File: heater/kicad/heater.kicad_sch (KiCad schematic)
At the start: 80 parts, among them J1 Conn_01x02_Pin, J2 Conn_01x02_Pin, J3 pcie_98, U1 OPA863SIDBVR, U11 ESD5344D-TP, U12 ESD5344D-TP, U13 XC6206P332MR, U14 B0505MT-1WR4, U15 TPS7A2025PDBVR, U16 LM27761, U3 LTC1968, U4 LTC1968, U8 ADS1115IDGS, U9 ISO1541

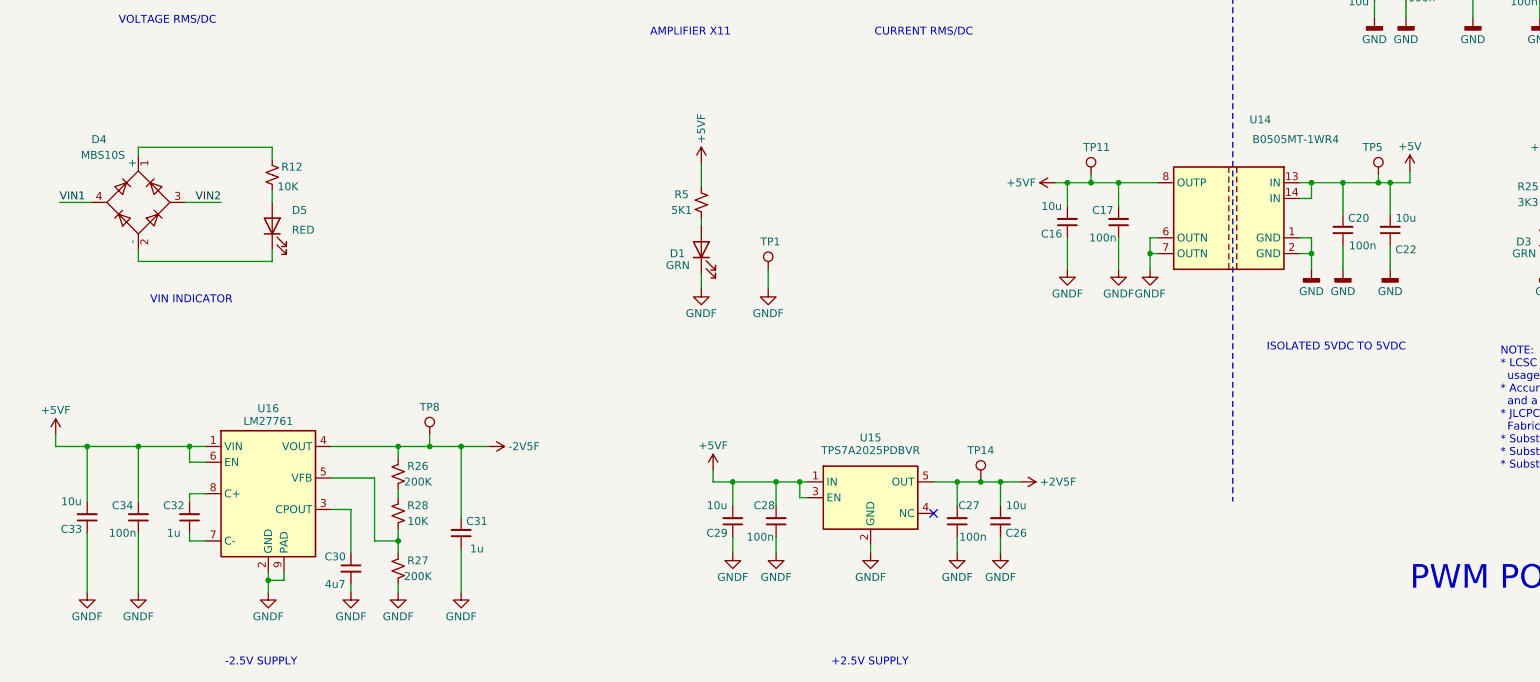
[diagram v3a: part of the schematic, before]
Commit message: Updated the heater schematic. Using +/-5V dc/dc instead of a charge pump.
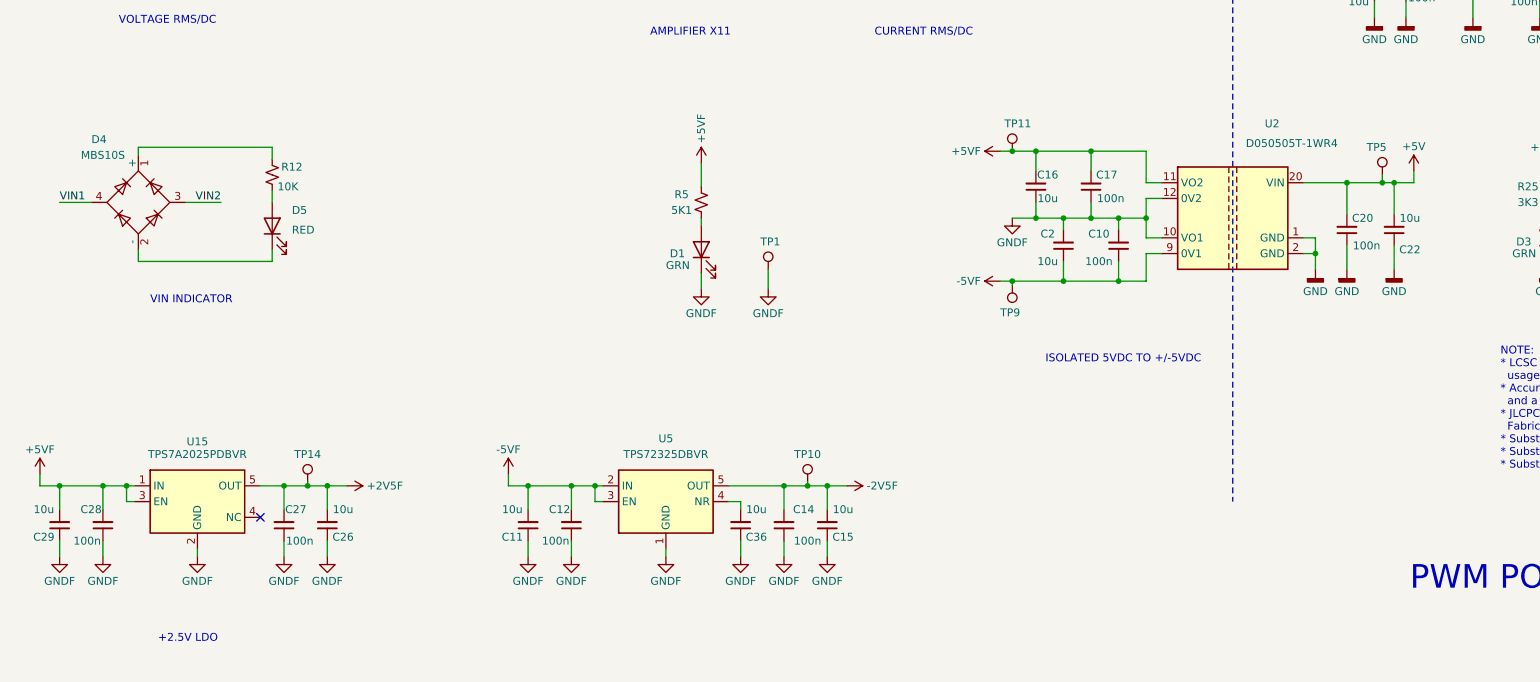
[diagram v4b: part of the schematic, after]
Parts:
- removed C30: 4u7, Capacitor_SMD:C_0402_1005Metric, symbol Device:C_Small
- removed C31, C32: 1u, Capacitor_SMD:C_0402_1005Metric, symbol Device:C_Small
- removed C33: 10u, Capacitor_SMD:C_0603_1608Metric, symbol Device:C_Small
- removed C34: 100n, Capacitor_SMD:C_0402_1005Metric, symbol Device:C_Small
- removed R26, R27: 200K, Resistor_SMD:R_0402_1005Metric, symbol Device:R_Small_US
- removed R28: 10K, Resistor_SMD:R_0402_1005Metric, symbol Device:R_Small_US
- removed TP8: TestPoint, common:Test_Pad, symbol common:TestPoint
- removed U14: B0505MT-1WR4, common:B0505MT-1WR4, symbol common:B0505MT-1WR4
- removed U16: LM27761, Package_SON:WSON-8-1EP_2x2mm_P0.5mm_EP0.9x1.6mm, symbol Regulator_SwitchedCapacitor:LM27761
- added C10, C12, C14: 100n, Capacitor_SMD:C_0402_1005Metric, symbol Device:C_Small
- added C11, C15, C2, C36: 10u, Capacitor_SMD:C_0603_1608Metric, symbol Device:C_Small
- added TP10, TP9: TestPoint, common:Test_Pad, symbol common:TestPoint
- added U2: D050505T-1WR4, common:D050505T-1WR4, symbol common:D050505T-1WR4
- added U5: TPS72325DBVR, Package_TO_SOT_SMD:SOT-23-5, symbol common:TPS72325DBVR
- U8: LCSC Digikey -> C37593
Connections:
- net +5V: now also U2.20 (VIN)
- net +5VF: now also U2.11 (VO2)
- net -2V5F: now also C14.2, C15.2, TP10.1, U5.5 (OUT)
- net GND: now also U2.1 (GND), U2.2 (GND)
- net GNDF: now also C10.2, C11.1, C12.1, C14.1, C15.1, C2.2, C36.1, U2.10 (VO1), U2.12 (0V2), U5.1 (GND)
- new net: C36.2, U5.4 (NR)
- new net -5VF: C10.1, C11.2, C12.2, C2.1, TP9.1, U2.9 (0V1), U5.2 (IN), U5.3 (EN)
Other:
- note added: "+2.5V LDO"
- note added: "ISOLATED 5VDC TO +/-5VDC"
- note removed: "+2.5V SUPPLY"
- note removed: "-2.5V SUPPLY"
- note removed: "ISOLATED 5VDC TO 5VDC"
- moved on the sheet: C16, C17, C20, C22, C26, C27, C28, C29, TP11, TP14, TP5, U15

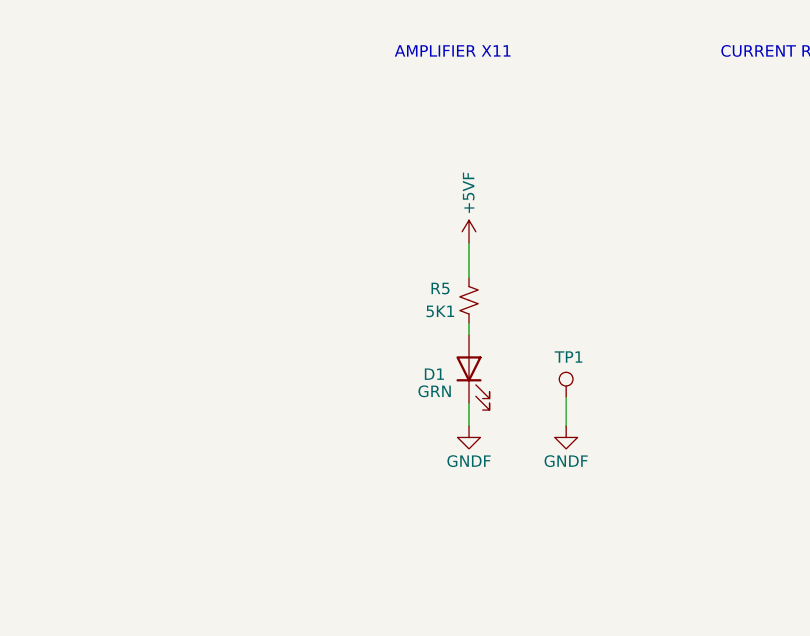
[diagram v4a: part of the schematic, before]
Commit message: Cleaned up the heater layout.
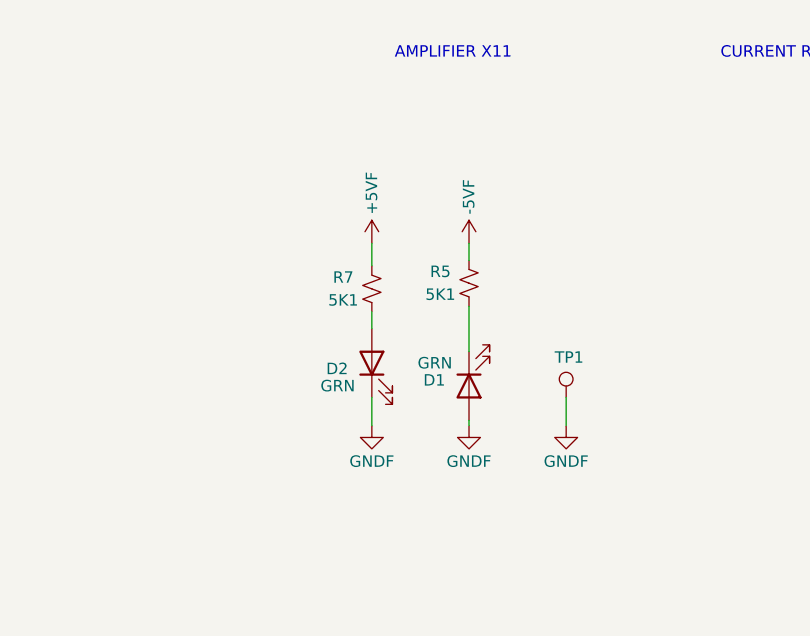
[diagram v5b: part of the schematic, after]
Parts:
- added D2: GRN, LED_SMD:LED_0603_1608Metric, symbol Device:LED
- added R7: 5K1, Resistor_SMD:R_0402_1005Metric, symbol Device:R_Small_US
- D4, U8: JLCRotOffset (none) -> 270
- U5: JLCRotOffset (none) -> 180
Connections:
- net +5VF: now also R7.1; no longer R5.1
- net -5VF: now also R5.1
- net GNDF: now also D1.2 (A), D2.1 (K); no longer D1.1 (K)
- net at R5.2: now also D1.1 (K); no longer D1.2 (A)
- new net: D2.2 (A), R7.2
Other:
- moved on the sheet: D1, R5
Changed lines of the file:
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@@
     (stroke (width 0) (type default))
   )
-  (wire (pts (xy 153.67 186.055) (xy 153.67 187.325))
+  (wire (pts (xy 153.67 184.15) (xy 153.67 189.23))
     (stroke (width 0) (type default))
   )
@@
     (stroke (width 0) (type default))
   )
-  (wire (pts (xy 153.67 177.165) (xy 153.67 180.975))
+  (wire (pts (xy 142.875 184.785) (xy 142.875 186.69))
+    (stroke (width 0) (type default))
+  )
+  (wire (pts (xy 153.67 177.165) (xy 153.67 179.07))
     (stroke (width 0) (type default))
   )
@@
     (stroke (width 0) (type default))
   )
+  (wire (pts (xy 142.875 177.165) (xy 142.875 179.705))
+    (stroke (width 0) (type default))
+  )
   (wire (pts (xy 89.535 76.2) (xy 100.965 76.2))
     (stroke (width 0) (type default))
@@
     (stroke (width 0) (type default))
   )
-  (wire (pts (xy 153.67 194.945) (xy 153.67 197.485))
+  (wire (pts (xy 153.67 196.85) (xy 153.67 197.485))
     (stroke (width 0) (type default))
   )
@@
     (stroke (width 0) (type default))
   )
+  (wire (pts (xy 142.875 194.31) (xy 142.875 197.485))
+    (stroke (width 0) (type default))
+  )
   (wire (pts (xy 290.195 193.04) (xy 290.195 194.31))
     (stroke (width 0) (type default))
@@
     )
   )
+  (symbol (lib_id "Device:R_Small_US") (at 142.875 182.245 0) (unit 1)
+    (in_bom yes) (on_board yes) (dnp no)
+    (property "Reference" "R7" (at 139.7 180.975 0)
+      (effects (font (size 1.27 1.27)))
+    )
+    (property "Value" "5K1" (at 139.7 183.515 0)
+      (effects (font (size 1.27 1.27)))
+    )
+    (property "Footprint" "Resistor_SMD:R_0402_1005Metric" (at 142.875 182.245 0)
+      (effects (font (size 1.27 1.27)) hide)
+    )
+    (property "Datasheet" "~" (at 142.875 182.245 0)
+      (effects (font (size 1.27 1.27)) hide)
+    )
+    (property "LCSC" "C25905" (at 142.875 182.245 0)
+      (effects (font (size 1.27 1.27)) hide)
+    )
+    (pin "1")
+    (pin "2")
+    (instances
+      (project "heater"
+        (path "/20ea543f-efab-45c2-9faf-6629ee17c3db"
+          (reference "R7") (unit 1)
+        )
+      )
+    )
+  )
   (symbol (lib_id "Device:C_Small") (at 173.99 235.585 180) (unit 1)
     (in_bom yes) (on_board yes) (dnp no)
@@
       (effects (font (size 1.27 1.27)) hide)
     )
+    (property "JLCRotOffset" "270" (at 62.865 183.515 90)
+      (effects (font (size 1.27 1.27)) hide)
+    )
     (pin "1")
     (pin "2")
@@
       (effects (font (size 1.27 1.27)) hide)
     )
+    (property "JLCRotOffset" "270" (at 168.91 67.945 0)
+      (effects (font (size 1.27 1.27)) hide)
+    )
     (pin "1")
     (pin "10")
@@
   )
   (symbol (lib_id "heater:-5VF") (at 201.93 196.215 90) (unit 1)
-    (in_bom yes) (on_board yes) (dnp no) (fields_autoplaced)
+    (in_bom yes) (on_board yes) (dnp no)
     (property "Reference" "#PWR07" (at 205.74 196.215 0)
       (effects (font (size 1.27 1.27)) hide)
@@
     )
   )
+  (symbol (lib_id "Device:LED") (at 142.875 190.5 90) (unit 1)
+    (in_bom yes) (on_board yes) (dnp no)
+    (property "Reference" "D2" (at 137.795 191.135 90)
+      (effects (font (size 1.27 1.27)) (justify right))
+    )
+    (property "Value" "GRN" (at 137.16 193.04 90)
+      (effects (font (size 1.27 1.27)) (justify right))
+    )
+    (property "Footprint" "LED_SMD:LED_0603_1608Metric" (at 142.875 190.5 0)
+      (effects (font (size 1.27 1.27)) hide)
+    )
+    (property "Datasheet" "~" (at 142.875 190.5 0)
+      (effects (font (size 1.27 1.27)) hide)
+    )
+    (property "LCSC" "C72043" (at 142.875 190.5 0)
+      (effects (font (size 1.27 1.27)) hide)
+    )
+    (pin "1")
+    (pin "2")
+    (instances
+      (project "heater"
+        (path "/20ea543f-efab-45c2-9faf-6629ee17c3db"
+          (reference "D2") (unit 1)
+        )
+      )
+    )
+  )
   (symbol (lib_id "Device:C_Small") (at 167.005 235.585 0) (mirror x) (unit 1)
     (in_bom yes) (on_board yes) (dnp no)
@@
     )
   )
+  (symbol (lib_id "heater:GNDF") (at 142.875 197.485 0) (mirror y) (unit 1)
+    (in_bom yes) (on_board yes) (dnp no) (fields_autoplaced)
+    (property "Reference" "#PWR044" (at 142.875 203.835 0)
+      (effects (font (size 1.27 1.27)) hide)
+    )
+    (property "Value" "GNDF" (at 142.875 201.43 0)
+      (effects (font (size 1.27 1.27)))
+    )
+    (property "Footprint" "" (at 142.875 197.485 0)
+      (effects (font (size 1.27 1.27)) hide)
+    )
+    (property "Datasheet" "" (at 142.875 197.485 0)
+      (effects (font (size 1.27 1.27)) hide)
+    )
+    (pin "1")
+    (instances
+      (project "heater"
+        (path "/20ea543f-efab-45c2-9faf-6629ee17c3db"
+          (reference "#PWR044") (unit 1)
+        )
+      )
+    )
+  )
   (symbol (lib_id "heater:GNDF") (at 160.02 240.665 0) (mirror y) (unit 1)
     (in_bom yes) (on_board yes) (dnp no)
@@
     )
   )
+  (symbol (lib_id "heater:+5VF") (at 142.875 177.165 0) (mirror y) (unit 1)
+    (in_bom yes) (on_board yes) (dnp no)
+    (property "Reference" "#PWR043" (at 142.875 180.975 0)
+      (effects (font (size 1.27 1.27)) hide)
+    )
+    (property "Value" "+5VF" (at 142.875 173.99 90)
+      (effects (font (size 1.27 1.27)) (justify left))
+    )
+    (property "Footprint" "" (at 142.875 177.165 0)
+      (effects (font (size 1.27 1.27)) hide)
+    )
+    (property "Datasheet" "" (at 142.875 177.165 0)
+      (effects (font (size 1.27 1.27)) hide)
+    )
+    (pin "1")
+    (instances
+      (project "heater"
+        (path "/20ea543f-efab-45c2-9faf-6629ee17c3db"
+          (reference "#PWR043") (unit 1)
+        )
+      )
+    )
+  )
   (symbol (lib_id "common:TestPoint") (at 299.72 194.31 0) (unit 1)
     (in_bom no) (on_board yes) (dnp no)
@@
     )
   )
-  (symbol (lib_id "heater:+5VF") (at 153.67 177.165 0) (mirror y) (unit 1)
-    (in_bom yes) (on_board yes) (dnp no)
-    (property "Reference" "#PWR03" (at 153.67 180.975 0)
-      (effects (font (size 1.27 1.27)) hide)
-    )
-    (property "Value" "+5VF" (at 153.67 173.99 90)
-      (effects (font (size 1.27 1.27)) (justify left))
-    )
-    (property "Footprint" "" (at 153.67 177.165 0)
-      (effects (font (size 1.27 1.27)) hide)
-    )
-    (property "Datasheet" "" (at 153.67 177.165 0)
-      (effects (font (size 1.27 1.27)) hide)
-    )
-    (pin "1")
-    (instances
-      (project "heater"
-        (path "/20ea543f-efab-45c2-9faf-6629ee17c3db"
-          (reference "#PWR03") (unit 1)
-        )
-      )
-    )
-  )
   (symbol (lib_id "heater:GNDF") (at 80.645 144.78 0) (unit 1)
     (in_bom yes) (on_board yes) (dnp no) (fields_autoplaced)
@@
       (effects (font (size 1.27 1.27)) hide)
     )
+    (property "JLCRotOffset" "180" (at 147.955 231.775 0)
+      (effects (font (size 1.27 1.27)) hide)
+    )
     (pin "1")
     (pin "2")
@@
     )
   )
+  (symbol (lib_id "heater:-5VF") (at 153.67 177.165 0) (unit 1)
+    (in_bom yes) (on_board yes) (dnp no)
+    (property "Reference" "#PWR045" (at 153.67 180.975 0)
+      (effects (font (size 1.27 1.27)) hide)
+    )
+    (property "Value" "-5VF" (at 153.67 173.9901 90)
+      (effects (font (size 1.27 1.27)) (justify left))
+    )
+    (property "Footprint" "" (at 153.67 177.165 0)
+      (effects (font (size 1.27 1.27)) hide)
+    )
+    (property "Datasheet" "" (at 153.67 177.165 0)
+      (effects (font (size 1.27 1.27)) hide)
+    )
+    (pin "1")
+    (instances
+      (project "heater"
+        (path "/20ea543f-efab-45c2-9faf-6629ee17c3db"
+          (reference "#PWR045") (unit 1)
+        )
+      )
+    )
+  )
   (symbol (lib_id "Device:R_Small_US") (at 195.58 59.69 180) (unit 1)
     (in_bom yes) (on_board yes) (dnp no)
@@
     )
   )
-  (symbol (lib_id "Device:LED") (at 153.67 191.135 90) (unit 1)
+  (symbol (lib_id "Device:LED") (at 153.67 193.04 90) (mirror x) (unit 1)
     (in_bom yes) (on_board yes) (dnp no)
-    (property "Reference" "D1" (at 148.59 191.77 90)
+    (property "Reference" "D1" (at 148.59 192.405 90)
       (effects (font (size 1.27 1.27)) (justify right))
     )
-    (property "Value" "GRN" (at 147.955 193.675 90)
+    (property "Value" "GRN" (at 147.955 190.5 90)
       (effects (font (size 1.27 1.27)) (justify right))
     )
-    (property "Footprint" "LED_SMD:LED_0603_1608Metric" (at 153.67 191.135 0)
+    (property "Footprint" "LED_SMD:LED_0603_1608Metric" (at 153.67 193.04 0)
       (effects (font (size 1.27 1.27)) hide)
     )
-    (property "Datasheet" "~" (at 153.67 191.135 0)
+    (property "Datasheet" "~" (at 153.67 193.04 0)
       (effects (font (size 1.27 1.27)) hide)
     )
-    (property "LCSC" "C72043" (at 153.67 191.135 0)
+    (property "LCSC" "C72043" (at 153.67 193.04 0)
       (effects (font (size 1.27 1.27)) hide)
     )
@@
     )
   )
-  (symbol (lib_id "Device:R_Small_US") (at 153.67 183.515 0) (unit 1)
+  (symbol (lib_id "Device:R_Small_US") (at 153.67 181.61 0) (unit 1)
     (in_bom yes) (on_board yes) (dnp no)
-    (property "Reference" "R5" (at 150.495 182.245 0)
+    (property "Reference" "R5" (at 150.495 180.34 0)
       (effects (font (size 1.27 1.27)))
     )
-    (property "Value" "5K1" (at 150.495 184.785 0)
+    (property "Value" "5K1" (at 150.495 182.88 0)
       (effects (font (size 1.27 1.27)))
     )
-    (property "Footprint" "Resistor_SMD:R_0402_1005Metric" (at 153.67 183.515 0)
+    (property "Footprint" "Resistor_SMD:R_0402_1005Metric" (at 153.67 181.61 0)
       (effects (font (size 1.27 1.27)) hide)
     )
-    (property "Datasheet" "~" (at 153.67 183.515 0)
+    (property "Datasheet" "~" (at 153.67 181.61 0)
       (effects (font (size 1.27 1.27)) hide)
     )
-    (property "LCSC" "C25905" (at 153.67 183.515 0)
+    (property "LCSC" "C25905" (at 153.67 181.61 0)
       (effects (font (size 1.27 1.27)) hide)
     )
